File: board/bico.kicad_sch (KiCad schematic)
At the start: 50 parts

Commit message: ERC clean. Split RP2040 DVDDs, and add LEDs and probe debug header
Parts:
- added D3, D4: LED, symbol Device:LED
- added J4: Conn_01x03, symbol Connector_Generic:Conn_01x03
- added R11, R12: 5k1, symbol Device:R_Small
- gave numbers to parts that had none: 46
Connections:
- net M_QSPI_CLK is gone; now on net M_QSPI_SCK: U2.6 (CLK)
- net P_QSPI_CLK is gone; now on net P_QSPI_SCK: U5.6 (CLK)
- net GND: now also J3.33 (Pin_33), J4.3 (Pin_3), R11.2, R12.2
- net LED: now also D3.2 (A)
- net P_LED: now also D4.2 (A)
- net P_SWCLK: now also J4.2 (Pin_2)
- net P_SWDIO: now also J4.1 (Pin_1)
- net +1V1 renamed DVDD_M
- net DVDD_M: no longer C13.1, C14.1, C15.1, U4.23 (DVDD), U4.45 (LDO_VOUT), U4.50 (DVDD)
- new net: D4.1 (K), R12.1
- new net: D3.1 (K), R11.1
- new net DVDD_P: C13.1, C14.1, C15.1, U4.23 (DVDD), U4.45 (LDO_VOUT), U4.50 (DVDD)
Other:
- note added: "GPIO assignments here match the stock picoprobe firmware."
- note added: "IO Headers"
- note added: "IOVDD + ADC_IOVDD Decoupling"
- note added: "Main uC does not have a crystal -- the crystal belongs to the probe uC, which is always running, and buffers the output on a GPCLK pin for use by the main uC."
- note added: "Probe debug port -- just a small (e.g. 0.05") unpopulated pin header, as the use cases for this are few"
- note added: "Some GPIOs are internal-only on Pico: 23: SMPS mode 24: VBUS detect 25: LED 29: VSYS ADC measurement We reuse these to provide UART + a spare GPIO connected directly to the probe uC. To get correct UART pin assignment, the LED has to move to GPIO 23."
- note added: "USB + Power"
- note removed: "Main uC does not have a crystal -- the single crystal belongs to the probe uC (which is always running), which buffers the output on a GPCLK pin for use by the main uC."
- moved on the sheet: C1, C10, C11, C12, C13, C14, C15, C16, C17, C18, C19, C2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

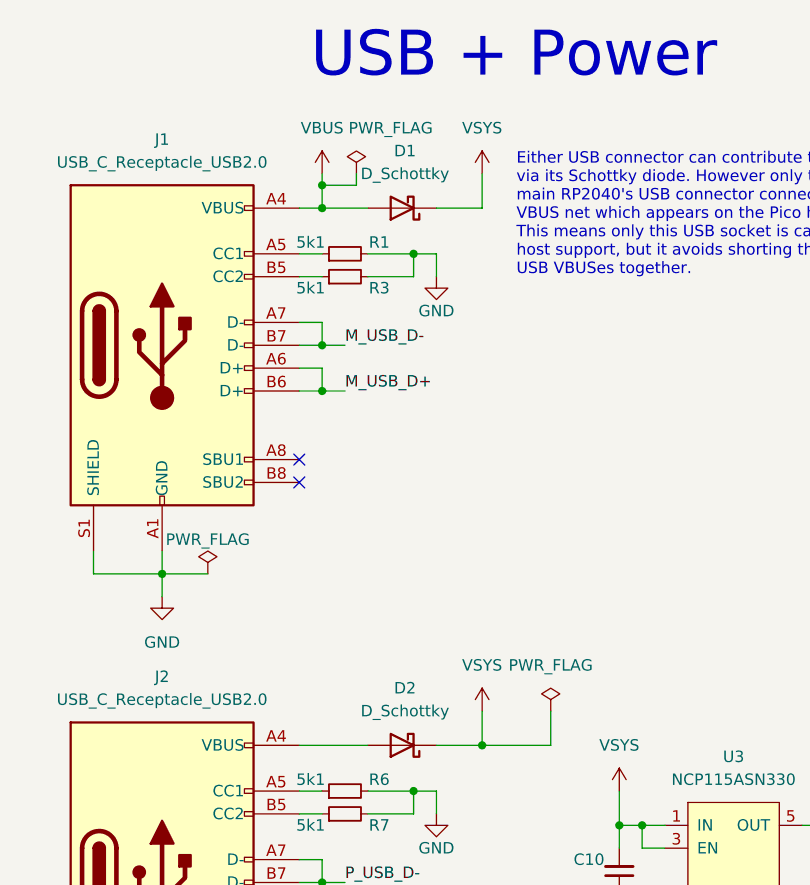
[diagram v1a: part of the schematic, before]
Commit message: Assign footprints
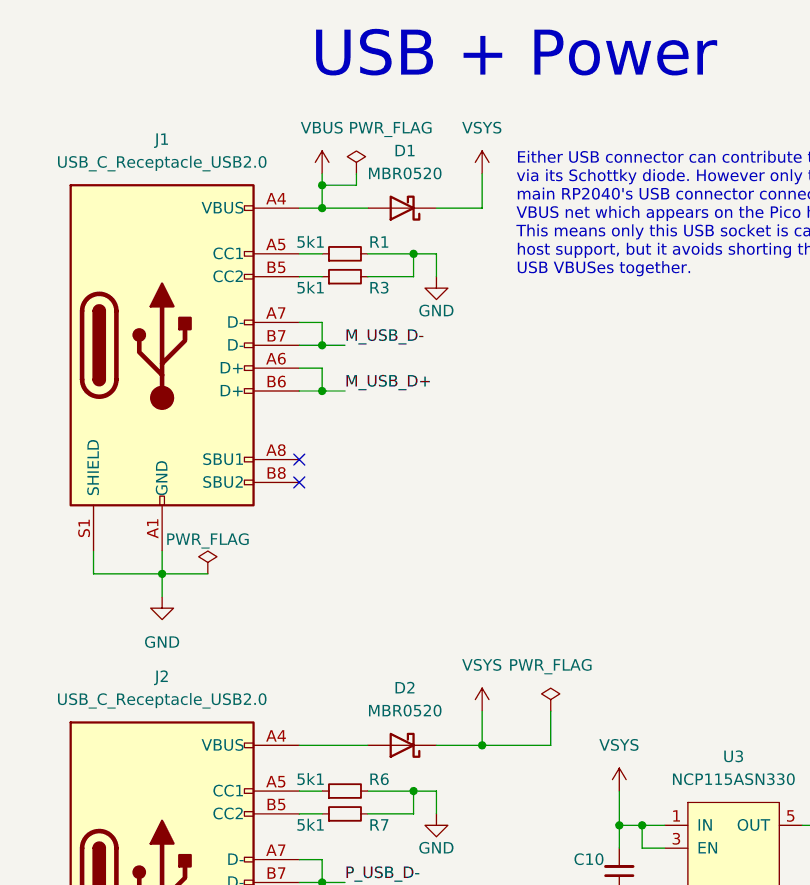
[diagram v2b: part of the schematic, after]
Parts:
- C1, C10, C11, C12, C13, C14, C15, C16, C17, C18, C19, C2, C20, C21, C22, C3, C4, C5, C6, C7, C8, C9: footprint (none) -> Capacitor_SMD:C_0402_1005Metric
- D1, D2: value D_Schottky -> MBR0520; footprint (none) -> Diode_SMD:D_SOD-123
- D3, D4: footprint (none) -> LED_SMD:LED_0603_1608Metric
- J1, J2: footprint (none) -> Connector_USB:USB_C_Receptacle_GCT_USB4105-xx-A_16P_TopMnt_Horizontal
- J3: footprint (none) -> bico:Pico_Headers
- J4: footprint (none) -> Connector_PinHeader_1.27mm:PinHeader_1x03_P1.27mm_Vertical
- R1, R10, R11, R12, R2, R3, R4, R5, R6, R7, R8, R9: footprint (none) -> Resistor_SMD:R_0402_1005Metric
- SW1, SW2, SW3: footprint (none) -> bico:SW_SPST_PTS815
- U1, U4: footprint (none) -> bico:QFN-56_EP_7x7_Pitch0.4mm
- U3: footprint (none) -> Package_TO_SOT_SMD:SOT-23-5_HandSoldering
- Y1: footprint (none) -> Crystal:Crystal_SMD_3225-4Pin_3.2x2.5mm

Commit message: Rough initial placement
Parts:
- U2, U5: footprint Package_SO:SOIC-8_5.23x5.23mm_P1.27mm -> bico:DFN-8-3x2mm-Winbond
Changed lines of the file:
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@@
       (effects (font (size 1.27 1.27)) (justify left))
     )
-    (property "Footprint" "Package_SO:SOIC-8_5.23x5.23mm_P1.27mm" (id 2) (at 207.01 73.66 0)
+    (property "Footprint" "bico:DFN-8-3x2mm-Winbond" (id 2) (at 207.01 73.66 0)
       (effects (font (size 1.27 1.27)) hide)
     )
@@
       (effects (font (size 1.27 1.27)) (justify left))
     )
-    (property "Footprint" "Package_SO:SOIC-8_5.23x5.23mm_P1.27mm" (id 2) (at 207.01 207.01 0)
+    (property "Footprint" "bico:DFN-8-3x2mm-Winbond" (id 2) (at 207.01 207.01 0)
       (effects (font (size 1.27 1.27)) hide)
     )
@@
     )
     (path "/6cf0019e-42d5-49cf-9a57-3b7aca24dcd9"
-      (reference "U2") (unit 1) (value "W25Q16JV") (footprint "Package_SO:SOIC-8_5.23x5.23mm_P1.27mm")
+      (reference "U2") (unit 1) (value "W25Q16JV") (footprint "bico:DFN-8-3x2mm-Winbond")
     )
     (path "/46f34ccb-4f0b-4b0d-8371-6660c6b0977b"
@@
     )
     (path "/b82d005f-3648-4bbb-a30e-91658aabb3b6"
-      (reference "U5") (unit 1) (value "W25Q16JV") (footprint "Package_SO:SOIC-8_5.23x5.23mm_P1.27mm")
+      (reference "U5") (unit 1) (value "W25Q16JV") (footprint "bico:DFN-8-3x2mm-Winbond")
     )
     (path "/2dc20fc9-0eda-4b72-ba41-2197371b37af"

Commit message: Start routing
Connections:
- net GND: now also SW1.2, SW2.1; no longer SW1.1, SW2.2
- net M_~{RST}: now also SW1.1; no longer SW1.2
- net at R5.2: now also SW2.2; no longer SW2.1
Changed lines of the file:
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@@
     (pin "56")
   )
-  (symbol (lib_id "Switch:SW_Push") (at 181.61 91.44 90) (unit 1)
+  (symbol (lib_id "Switch:SW_Push") (at 181.61 91.44 90) (mirror x) (unit 1)
     (in_bom yes) (on_board yes) (fields_autoplaced)
     (property "Reference" "SW1" (id 0) (at 182.88 90.1699 90)
@@
     (pin "2")
   )
-  (symbol (lib_id "Switch:SW_Push") (at 191.77 91.44 270) (unit 1)
+  (symbol (lib_id "Switch:SW_Push") (at 191.77 91.44 270) (mirror x) (unit 1)
     (in_bom yes) (on_board yes) (fields_autoplaced)
     (property "Reference" "SW2" (id 0) (at 195.58 90.1699 90)

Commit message: Fully routed
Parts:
- J4: footprint Connector_PinHeader_1.27mm:PinHeader_1x03_P1.27mm_Vertical -> Connector_PinHeader_1.00mm:PinHeader_1x03_P1.00mm_Vertical
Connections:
- net GND: now also D4.1 (K); no longer R12.2
- net P_LED: now also R12.1; no longer D4.2 (A), U4.9 (GPIO7)
- new net: D4.2 (A), R12.2
- no-connect marks 29 -> 30
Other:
- moved on the sheet: D4, R12
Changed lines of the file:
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@@
   (no_connect (at 114.3 223.52))
   (no_connect (at 114.3 248.92))
+  (no_connect (at 114.3 210.82))
   (no_connect (at 361.95 204.47))
   (no_connect (at 330.2 71.12))
@@
     (stroke (width 0) (type default) (color 0 0 0 0))
   )
-  (wire (pts (xy 114.3 210.82) (xy 116.84 210.82))
-    (stroke (width 0) (type default) (color 0 0 0 0))
-  )
   (wire (pts (xy 328.93 232.41) (xy 334.01 232.41))
     (stroke (width 0) (type default) (color 0 0 0 0))
@@
     (stroke (width 0) (type default) (color 0 0 0 0))
   )
-  (wire (pts (xy 238.76 248.92) (xy 238.76 251.46))
+  (wire (pts (xy 238.76 246.38) (xy 238.76 248.92))
     (stroke (width 0) (type default) (color 0 0 0 0))
   )
@@
     (effects (font (size 1.27 1.27)) (justify right bottom))
   )
-  (label "P_LED" (at 116.84 210.82 0)
-    (effects (font (size 1.27 1.27)) (justify left bottom))
-  )
   (label "GPIO4" (at 328.93 204.47 180)
     (effects (font (size 1.27 1.27)) (justify right bottom))
@@
     (pin "1")
   )
-  (symbol (lib_id "Device:LED") (at 238.76 245.11 90) (unit 1)
+  (symbol (lib_id "Device:LED") (at 238.76 252.73 90) (unit 1)
     (in_bom yes) (on_board yes) (fields_autoplaced)
-    (property "Reference" "D4" (id 0) (at 242.57 245.4274 90)
+    (property "Reference" "D4" (id 0) (at 242.57 253.0474 90)
       (effects (font (size 1.27 1.27)) (justify right))
     )
-    (property "Value" "LED" (id 1) (at 242.57 247.9674 90)
+    (property "Value" "LED" (id 1) (at 242.57 255.5874 90)
       (effects (font (size 1.27 1.27)) (justify right))
     )
-    (property "Footprint" "LED_SMD:LED_0603_1608Metric" (id 2) (at 238.76 245.11 0)
+    (property "Footprint" "LED_SMD:LED_0603_1608Metric" (id 2) (at 238.76 252.73 0)
       (effects (font (size 1.27 1.27)) hide)
     )
-    (property "Datasheet" "~" (id 3) (at 238.76 245.11 0)
+    (property "Datasheet" "~" (id 3) (at 238.76 252.73 0)
       (effects (font (size 1.27 1.27)) hide)
     )
@@
     (pin "1")
   )
-  (symbol (lib_id "Device:R_Small") (at 238.76 254 0) (unit 1)
+  (symbol (lib_id "Device:R_Small") (at 238.76 243.84 0) (unit 1)
     (in_bom yes) (on_board yes)
-    (property "Reference" "R12" (id 0) (at 233.68 252.73 0)
+    (property "Reference" "R12" (id 0) (at 233.68 242.57 0)
       (effects (font (size 1.27 1.27)) (justify left))
     )
-    (property "Value" "5k1" (id 1) (at 233.68 255.27 0)
+    (property "Value" "5k1" (id 1) (at 233.68 245.11 0)
       (effects (font (size 1.27 1.27)) (justify left))
     )
-    (property "Footprint" "Resistor_SMD:R_0402_1005Metric" (id 2) (at 238.76 254 0)
+    (property "Footprint" "Resistor_SMD:R_0402_1005Metric" (id 2) (at 238.76 243.84 0)
       (effects (font (size 1.27 1.27)) hide)
     )
-    (property "Datasheet" "~" (id 3) (at 238.76 254 0)
+    (property "Datasheet" "~" (id 3) (at 238.76 243.84 0)
       (effects (font (size 1.27 1.27)) hide)
     )
@@
       (effects (font (size 1.27 1.27)) (justify left))
     )
-    (property "Footprint" "Connector_PinHeader_1.27mm:PinHeader_1x03_P1.27mm_Vertical" (id 2) (at 299.72 237.49 0)
+    (property "Footprint" "Connector_PinHeader_1.00mm:PinHeader_1x03_P1.00mm_Vertical" (id 2) (at 299.72 237.49 0)
       (effects (font (size 1.27 1.27)) hide)
     )
@@
     )
     (path "/a7849bb2-581a-4cd9-bb1f-e025ca912bff"
-      (reference "J4") (unit 1) (value "Conn_01x03") (footprint "Connector_PinHeader_1.27mm:PinHeader_1x03_P1.27mm_Vertical")
+      (reference "J4") (unit 1) (value "Conn_01x03") (footprint "Connector_PinHeader_1.00mm:PinHeader_1x03_P1.00mm_Vertical")
     )
     (path "/20331a56-8e54-4abf-a2bb-bacedbdc7240"

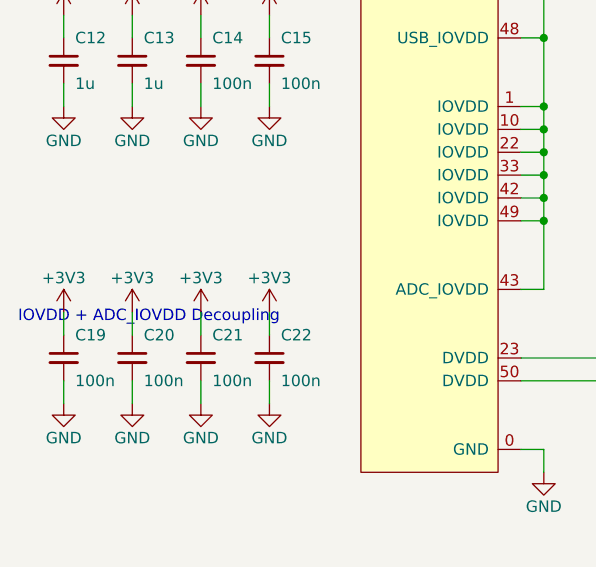
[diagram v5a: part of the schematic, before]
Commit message: Label all pins in silkscreen
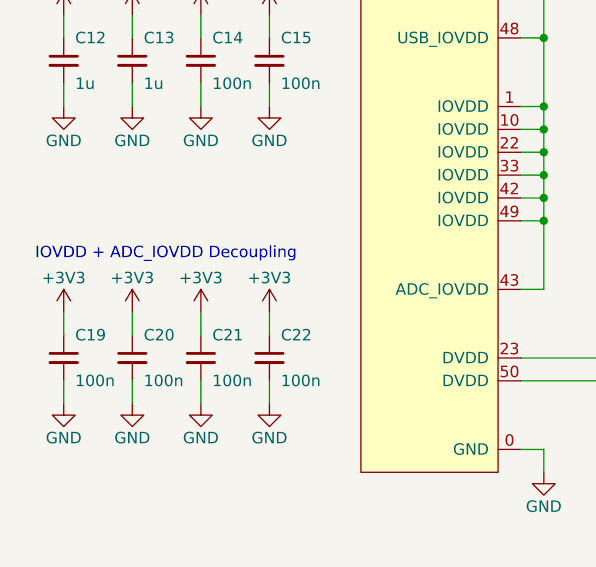
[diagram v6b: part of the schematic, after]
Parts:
- C1, C10, C11, C12, C13, C14, C15, C16, C17, C18, C19, C2, C20, C21, C22, C3, C4, C5, C6, C7, C8, C9: footprint Capacitor_SMD:C_0402_1005Metric -> bico:C_0402_1005Metric
- D1, D2: footprint Diode_SMD:D_SOD-123 -> bico:D_SOD-123
- D3, D4: footprint LED_SMD:LED_0603_1608Metric -> bico:LED_0603_1608Metric
- J4: footprint Connector_PinHeader_1.00mm:PinHeader_1x03_P1.00mm_Vertical -> bico:PinHeader_1x03_P1.00mm_Vertical
- R1, R10, R11, R12, R2, R3, R4, R5, R6, R7, R8, R9: footprint Resistor_SMD:R_0402_1005Metric -> bico:R_0402_1005Metric
- U3: footprint Package_TO_SOT_SMD:SOT-23-5_HandSoldering -> bico:SOT-23-5_HandSoldering
